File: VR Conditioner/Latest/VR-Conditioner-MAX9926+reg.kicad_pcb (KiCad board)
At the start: 2 copper layers, 19.7 x 19.7 mm, 22 parts, among them J1 8-pin header, J2 Edge, U1 MAX9926UAEE+, U2 AMS1117CD-5.0

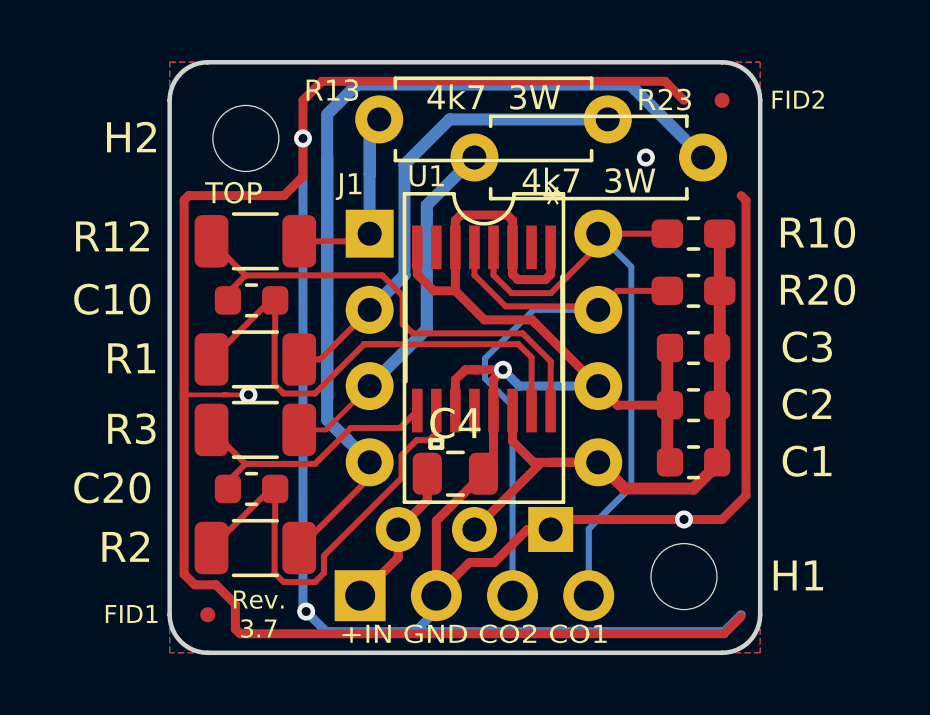
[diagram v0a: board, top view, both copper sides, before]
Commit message: Improve silk screen labeling & ground plane. Added solder pads.
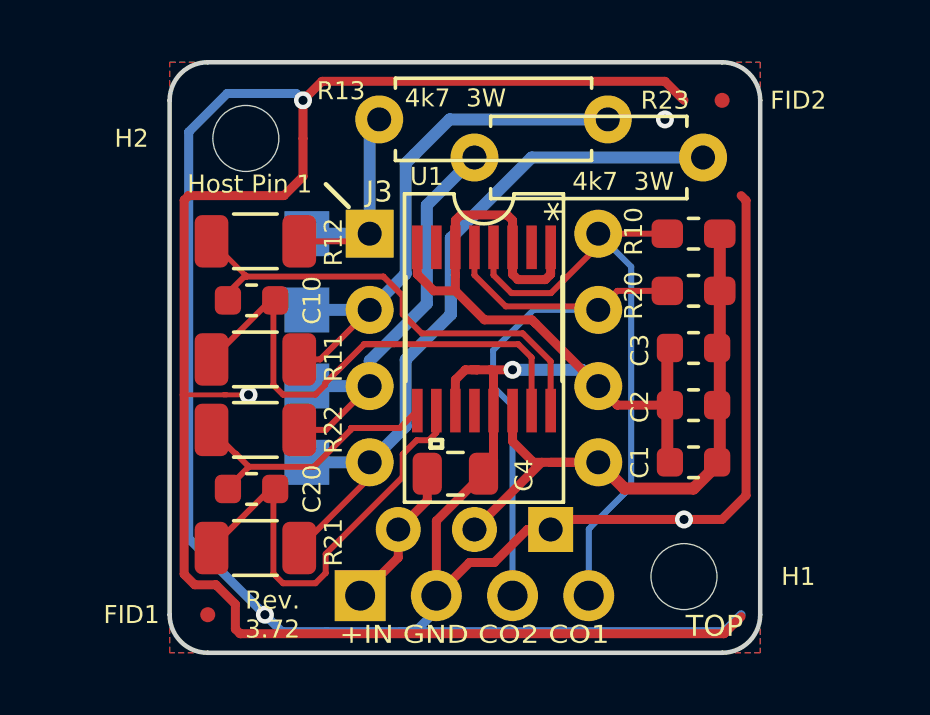
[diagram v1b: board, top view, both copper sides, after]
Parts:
- added TP1: TP, TestPoint:TestPoint_Pad_1.5x1.5mm, B.Cu at (117.0, 102.2)
- added TP2: TP, TestPoint:TestPoint_Pad_1.5x1.5mm, B.Cu at (117.0, 104.8)
- added TP3: TP, TestPoint:TestPoint_Pad_1.5x1.5mm, B.Cu at (117.0, 107.3)
- added TP4: TP, TestPoint:TestPoint_Pad_1.5x1.5mm, B.Cu at (117.0, 109.9)
- renumbered J1 to J3, R1 to R11, R2 to R21, R3 to R22
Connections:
- U1 pad 12: Net-(U1-Pad12) -> unconnected-(U1-Pad12)
- U1 pad 2: Net-(U1-Pad2) -> unconnected-(U1-Pad2)
- U1 pad 7: Net-(U1-Pad7) -> unconnected-(U1-Pad7)
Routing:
- net Net-(J3-Pad4): track 38.5 -> 25.0 mm
- net GND: track 148.7 -> 155.7 mm
- net Net-(J3-Pad2): track 15.8 -> 17.9 mm
- net Net-(J3-Pad3): track 12.0 -> 14.1 mm
- net Net-(C10-Pad1): track 17.0 -> 16.0 mm
- net Net-(J3-Pad1): track 7.60 -> 8.49 mm
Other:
- net class Default removed
- net class Minimum removed
- net class power removed
- board text added: "&MS"
- board text added: "Host Pin 1"
- board text added: "Rev. 3.72"
- board text added: "SoFar: + under 20x20mm & SMT components on only one side for ‘Letter’ postage. + M2 mounting holes + Optional power resisotrs + Optional regulator for typical automotive power + Optional pin header for breadboard etc. + Could cut at pin header for direct PCB mount by castellation 2021-04-24: Goal: Give left 6 passive components space from the left edge & the DIP Move signal trace away from right 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"
- board text added: "Speeduino"
- board text added: "compatible"
- board text removed: "Rev. 3.7"
- board text removed: "SoFar: + under 20x20mm & single sided for ‘Letter’ postage. + M2 mounting holes + Optional power resisotrs + Optional regulator for typical automotive power + Optional pin header for breadboard etc. + Could cut at pin header for direct PCB mount by castellation 2021424: Goal: Give left 6 passive components space from the left edge & the DIP Move signal trace away from right edge. Only traces by e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"
- board text removed: "Speeduino / compatible"
